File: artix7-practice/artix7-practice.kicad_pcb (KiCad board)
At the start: 2 copper layers, 49 parts, among them J101 USB_B_Micro, J102 Conn_02x06_Odd_Even, Q101 Q_NMOS_GSD, U102 TLV62568DDC, U103 TLV62568DDC, U104 FT2232HL, U105 93CxxC, U106 W25Q128JVS, X101 125MHz, Y101 ABM8-272-T3

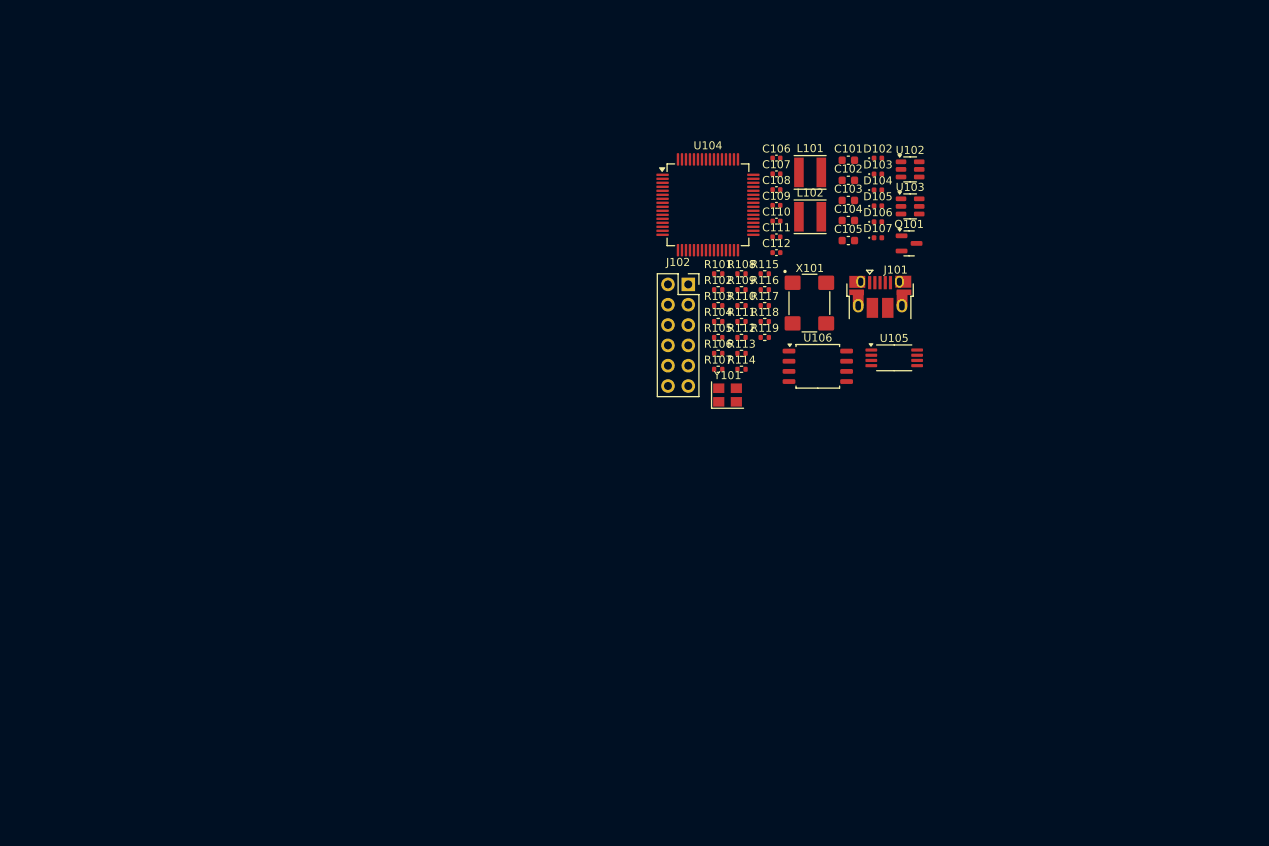
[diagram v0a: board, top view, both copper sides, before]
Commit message: Final version before switching from XC7A35T-xFTG256 to -xCSG325
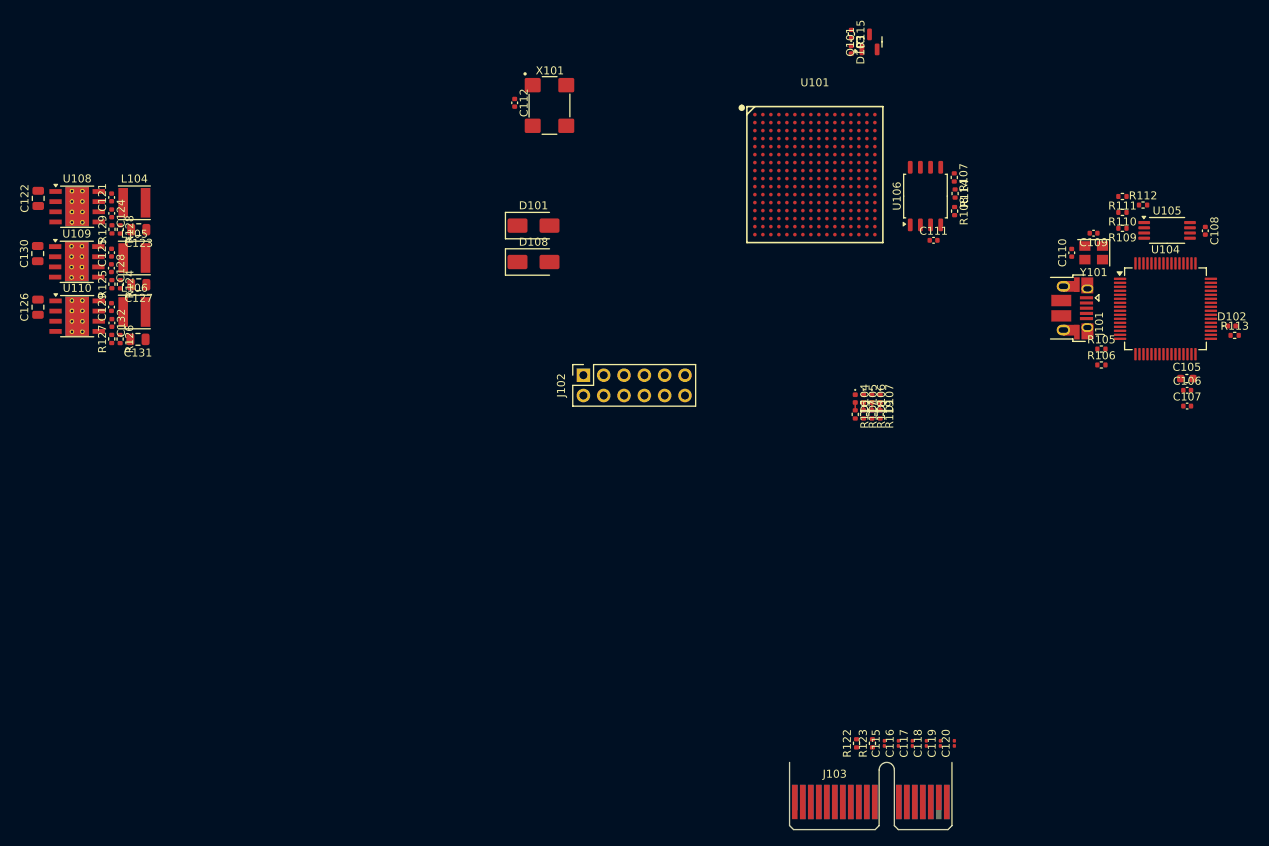
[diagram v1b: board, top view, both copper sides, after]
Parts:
- removed C101, C102, C103, C104: 22u, Capacitor_SMD:C_0603_1608Metric
- removed L101, L102: 2.2uH, Inductor_SMD:L_Taiyo-Yuden_NR-40xx
- removed R101: 39k, Resistor_SMD:R_0402_1005Metric
- removed R102: 62k, Resistor_SMD:R_0402_1005Metric
- removed R103: 68k, Resistor_SMD:R_0402_1005Metric
- removed R104: 33k, Resistor_SMD:R_0402_1005Metric
- removed U102, U103: TLV62568DDC, Package_TO_SOT_SMD:SOT-23-6
- added C115: 100n, Capacitor_SMD:C_0201_0603Metric, F.Cu at (63.3, 111.1)
- added C116: 100n, Capacitor_SMD:C_0201_0603Metric, F.Cu at (65.1, 111.1)
- added C117: 100n, Capacitor_SMD:C_0201_0603Metric, F.Cu at (66.8, 111.1)
- added C118: 100n, Capacitor_SMD:C_0201_0603Metric, F.Cu at (68.6, 111.1)
- added C119: 100n, Capacitor_SMD:C_0201_0603Metric, F.Cu at (70.3, 111.1)
- added C120: 100n, Capacitor_SMD:C_0201_0603Metric, F.Cu at (72.1, 111.1)
- added C121: 100n, Capacitor_SMD:C_0402_1005Metric, F.Cu at (-33.3, 42.9)
- added C122: 22u, Capacitor_SMD:C_0805_2012Metric, F.Cu at (-42.4, 43.0)
- added C123: 22u, Capacitor_SMD:C_0805_2012Metric, F.Cu at (-29.9, 46.9)
- added C124: 1u, Capacitor_SMD:C_0402_1005Metric, F.Cu at (-33.3, 44.9)
- added C125: 100n, Capacitor_SMD:C_0402_1005Metric, F.Cu at (-33.3, 49.8)
- added C126: 22u, Capacitor_SMD:C_0805_2012Metric, F.Cu at (-42.5, 56.6)
- added C127: 22u, Capacitor_SMD:C_0805_2012Metric, F.Cu at (-29.9, 53.8)
- added C128: 1u, Capacitor_SMD:C_0402_1005Metric, F.Cu at (-33.3, 51.7)
- added C129: 100n, Capacitor_SMD:C_0402_1005Metric, F.Cu at (-33.3, 56.6)
- added C130: 22u, Capacitor_SMD:C_0805_2012Metric, F.Cu at (-42.5, 49.9)
- added C131: 22u, Capacitor_SMD:C_0805_2012Metric, F.Cu at (-30.0, 60.6)
- added C132: 1u, Capacitor_SMD:C_0402_1005Metric, F.Cu at (-33.2, 58.6)
- added D101: MBRA340, Diode_SMD:D_SMA, F.Cu at (19.5, 46.4)
- added D108: MBRA340, Diode_SMD:D_SMA, F.Cu at (19.5, 51.0)
- added J103: Bus_PCI_Express_x1, Connector_PCBEdge:BUS_PCIexpress_x1, F.Cu at (52.1, 118.5)
- added L104: 2.2uH, Inductor_SMD:L_Taiyo-Yuden_NR-40xx, F.Cu at (-30.4, 43.6)
- added L105: 2.2uH, Inductor_SMD:L_Taiyo-Yuden_NR-40xx, F.Cu at (-30.4, 50.5)
- added L106: 2.2uH, Inductor_SMD:L_Taiyo-Yuden_NR-40xx, F.Cu at (-30.4, 57.2)
- added R122: 4.7k, Resistor_SMD:R_0402_1005Metric, F.Cu at (59.8, 111.1)
- added R123: 4.7k, Resistor_SMD:R_0402_1005Metric, F.Cu at (61.8, 111.1)
- added R124: 43k, Resistor_SMD:R_0402_1005Metric, F.Cu at (-32.2, 53.8)
- added R125: 56k, Resistor_SMD:R_0402_1005Metric, F.Cu at (-33.2, 53.7)
- added R126: 68k, Resistor_SMD:R_0402_1005Metric, F.Cu at (-32.2, 60.6)
- added R127: 30k, Resistor_SMD:R_0402_1005Metric, F.Cu at (-33.3, 60.6)
- added R128: 1k, Resistor_SMD:R_0402_1005Metric, F.Cu at (-32.2, 46.9)
- added R129: 150k, Resistor_SMD:R_0402_1005Metric, F.Cu at (-33.2, 46.9)
- added U101: XC7A35T-FTG256, easyeda2kicad:FBGA-256_L17.0-W17.0-R16-C16-P1.00-TL, F.Cu at (54.6, 40.0)
- added U108: LMR33630ADDA, Package_SO:Texas_HSOP-8-1EP_3.9x4.9mm_P1.27mm_ThermalVias, F.Cu at (-37.6, 44.1)
- added U109: LMR33630ADDA, Package_SO:Texas_HSOP-8-1EP_3.9x4.9mm_P1.27mm_ThermalVias, F.Cu at (-37.6, 51.0)
- added U110: LMR33630ADDA, Package_SO:Texas_HSOP-8-1EP_3.9x4.9mm_P1.27mm_ThermalVias, F.Cu at (-37.6, 57.7)
- moved R113 61.7 mm to (107.1, 60.1)
- moved C106 59.0 mm to (101.2, 67.0)
- moved C107 59.0 mm to (101.2, 69.0)
- moved U104 58.6 mm to (98.5, 56.8)
- moved C108 53.9 mm to (103.4, 47.1), turned to -90 degrees
- moved R112 52.9 mm to (95.7, 43.9)
- moved R111 50.1 mm to (93.1, 42.8), turned to 180 degrees
- moved Y101 49.1 mm to (89.5, 49.8), turned to 180 degrees
- moved R110 49.0 mm to (93.1, 44.8), turned to 180 degrees
- moved D102 49.0 mm to (106.8, 59.0)
- moved R109 48.2 mm to (93.1, 46.8), turned to 180 degrees
- moved R105 47.9 mm to (90.5, 61.9)
- moved R106 47.9 mm to (90.5, 63.8)
- moved C105 45.7 mm to (101.1, 65.5)
- moved X101 40.8 mm to (21.5, 31.4)
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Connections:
- J101 pad 1: +5V -> VBUS
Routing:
- net Net-(D107-A): track 0.00 -> 0.98 mm
- net Net-(D106-A): track 0.00 -> 0.98 mm
- net Net-(D105-A): track 0.00 -> 0.98 mm
- net Net-(D104-A): track 0.00 -> 0.98 mm
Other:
- board outline added: 20.3 x 8.4 mm

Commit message: JLCPCB uploads
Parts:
- added C101: 100n, Capacitor_SMD:C_0402_1005Metric, F.Cu at (71.0, 77.8)
- added C102: 22u, Capacitor_SMD:C_0805_2012Metric, F.Cu at (61.8, 77.9)
- added C103: 22u, Capacitor_SMD:C_0805_2012Metric, F.Cu at (74.3, 81.8)
- added C104: 1u, Capacitor_SMD:C_0402_1005Metric, F.Cu at (71.0, 79.8)
- added C113: 22u, Capacitor_SMD:C_0603_1608Metric, B.Cu at (82.4, 89.9)
- added C114: 22u, Capacitor_SMD:C_0603_1608Metric, B.Cu at (82.4, 93.6)
- added C133: 1u, Capacitor_SMD:C_0201_0603Metric, B.Cu at (87.9, 91.3)
- added C134: 1u, Capacitor_SMD:C_0201_0603Metric, B.Cu at (88.7, 93.7)
- added C135: 1u, Capacitor_SMD:C_0201_0603Metric, B.Cu at (85.5, 94.5)
- added C136: 1u, Capacitor_SMD:C_0201_0603Metric, B.Cu at (84.7, 92.1)
- added C137: 1u, Capacitor_SMD:C_0201_0603Metric, B.Cu at (85.5, 91.3)
- added C138: 100n, Capacitor_SMD:C_0201_0603Metric, B.Cu at (87.1, 91.3)
- added C139: 1u, Capacitor_SMD:C_0201_0603Metric, B.Cu at (93.9, 86.9)
- added C140: 100n, Capacitor_SMD:C_0201_0603Metric, B.Cu at (87.1, 94.5)
- added C141: 100n, Capacitor_SMD:C_0201_0603Metric, B.Cu at (83.9, 93.7)
- added C142: 1u, Capacitor_SMD:C_0201_0603Metric, B.Cu at (87.9, 92.9)
- added C143: 1u, Capacitor_SMD:C_0201_0603Metric, B.Cu at (90.7, 86.9)
- added C144: 100n, Capacitor_SMD:C_0201_0603Metric, B.Cu at (93.1, 87.7)
- added C145: 100n, Capacitor_SMD:C_0201_0603Metric, B.Cu at (88.3, 87.7)
- added C146: 1u, Capacitor_SMD:C_0201_0603Metric, B.Cu at (87.5, 86.9)
- added C147: 1u, Capacitor_SMD:C_0201_0603Metric, B.Cu at (89.1, 89.3)
- added C148: 100n, Capacitor_SMD:C_0201_0603Metric, B.Cu at (93.1, 90.1)
- added C149: 100n, Capacitor_SMD:C_0201_0603Metric, B.Cu at (88.3, 90.1)
- added C150: 1u, Capacitor_SMD:C_0201_0603Metric, B.Cu at (93.1, 89.3)
- added C151: 1u, Capacitor_SMD:C_0201_0603Metric, B.Cu at (91.5, 89.3)
- added C152: 100n, Capacitor_SMD:C_0201_0603Metric, B.Cu at (90.7, 90.1)
- added C153: 100n, Capacitor_SMD:C_0201_0603Metric, B.Cu at (92.3, 86.1)
- added C154: 1u, Capacitor_SMD:C_0201_0603Metric, B.Cu at (89.1, 85.3)
- added C155: 1u, Capacitor_SMD:C_0201_0603Metric, B.Cu at (90.7, 85.3)
- added C156: 1u, Capacitor_SMD:C_0201_0603Metric, B.Cu at (93.9, 85.3)
- added C157: 100n, Capacitor_SMD:C_0201_0603Metric, B.Cu at (92.3, 85.3)
- added C158: 1u, Capacitor_SMD:C_0201_0603Metric, B.Cu at (89.9, 87.7)
- added C159: 1u, Capacitor_SMD:C_0201_0603Metric, B.Cu at (95.5, 86.9)
- added C160: 1u, Capacitor_SMD:C_0201_0603Metric, B.Cu at (86.7, 86.1)
- added C161: 1u, Capacitor_SMD:C_0201_0603Metric, B.Cu at (94.3, 89.7)
- added C162: 22u, Capacitor_SMD:C_0603_1608Metric, B.Cu at (96.8, 91.3)
- added C163: 22u, Capacitor_SMD:C_0603_1608Metric, B.Cu at (92.1, 92.9)
- added C164: 22u, Capacitor_SMD:C_0603_1608Metric, B.Cu at (85.9, 82.8)
- added C165: 22u, Capacitor_SMD:C_0603_1608Metric, B.Cu at (93.9, 82.8)
- added L101: 2.2uH, Inductor_SMD:L_Taiyo-Yuden_NR-40xx, F.Cu at (73.8, 78.5)
- added L102: 2.2uH, Inductor_SMD:L_Taiyo-Yuden_NR-40xx, F.Cu at (79.5, 89.1)
- added L103: 2.2uH, Inductor_SMD:L_Taiyo-Yuden_NR-40xx, F.Cu at (79.4, 94.3)
- added R101: 18k, Resistor_SMD:R_0402_1005Metric, F.Cu at (72.1, 81.8)
- added R102: 82k, Resistor_SMD:R_0402_1005Metric, F.Cu at (71.0, 81.8)
- added R103: 100, Resistor_SMD:R_0402_1005Metric, B.Cu at (80.7, 89.9)
- added U102: XC7A35T-CSG325, Package_BGA:Xilinx_CSG325, F.Cu at (90.7, 88.1)
- C105, C106, C107, C109, C110, C111, C115, C116, C119, C120, R107, R108, R109, R111, R112, R114, X101, Y101: moved to B.Cu
- U101: value XC7A35T-FTG256 -> LMR33630ADDA; footprint easyeda2kicad:FBGA-256_L17.0-W17.0-R16-C16-P1.00-TL -> Package_SO:Texas_HSOP-8-1EP_3.9x4.9mm_P1.27mm_ThermalVias
- moved C126 109.8 mm to (61.7, 91.3)
- moved C127 109.8 mm to (74.3, 88.5)
- moved C128 109.8 mm to (70.9, 86.4)
- moved C129 109.8 mm to (70.9, 91.3)
- moved C130 109.8 mm to (61.7, 84.6)
- moved C132 109.8 mm to (71.0, 93.3)
- moved L105 109.8 mm to (73.8, 85.2)
- moved L106 109.8 mm to (73.8, 91.9)
- moved R124 109.8 mm to (72.0, 88.5)
- moved R125 109.8 mm to (71.0, 88.4)
- moved R126 109.8 mm to (72.0, 95.3)
- moved U109 109.8 mm to (66.6, 85.7)
- moved U110 109.8 mm to (66.6, 92.4)
- moved C125 109.8 mm to (70.9, 84.5)
- moved C131 109.8 mm to (74.2, 95.3)
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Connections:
- net Net-(J103-PERn0) renamed /PCIE_TX0_PRE-
- net Net-(J103-PERp0) renamed /PCIE_TX0_PRE+
- net Net-(J103-PETn0) renamed /PCIE_RX0_PRE-
- net Net-(J103-PETp0) renamed /PCIE_RX0_PRE+
- net Net-(J103-REFCLK+) renamed /REFCLK_PRE+
- net Net-(J103-REFCLK-) renamed /REFCLK_PRE-
- D101 pad 1: /POWER -> /MAIN_PWR
- D108 pad 1: /POWER -> /MAIN_PWR
- U108 pad 4: Net-(U108-PG) -> Net-(U101-EN)
- U109 pad 3: Net-(U108-PG) -> Net-(U101-EN)
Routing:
- net GND: track 0.00 -> 99.0 mm, vias 0 -> 127
- net /MAIN_PWR: track 0.00 -> 93.6 mm
- net +1V8: track 0.00 -> 63.2 mm, vias 0 -> 9
- net +3V3: track 0.00 -> 52.5 mm, vias 0 -> 42
- net +1V0: track 0.00 -> 49.2 mm, vias 0 -> 24
- net /JTAG_TMS: track 0.00 -> 47.7 mm, vias 0 -> 4
- net /JTAG_TDI: track 0.00 -> 47.2 mm, vias 0 -> 4
- net /JTAG_TDO: track 0.00 -> 46.3 mm, vias 0 -> 4
- net /GPIO0: track 0.00 -> 43.6 mm, vias 0 -> 1
- net /GPIO4: track 0.00 -> 43.5 mm, vias 0 -> 1
- net /GPIO5: track 0.00 -> 41.2 mm, vias 0 -> 1
- net /GPIO1: track 0.00 -> 40.0 mm, vias 0 -> 1
- net /GPIO6: track 0.00 -> 39.1 mm, vias 0 -> 1
- net /LED1: track 0.00 -> 38.1 mm, vias 0 -> 2
- net /LED2: track 0.00 -> 37.1 mm, vias 0 -> 2
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- added copper zone on F.Cu, net +12V
- added copper zone on In2.Cu, net +1V0
- added copper zone on In4.Cu, net +3V3
- added copper zone on In1.Cu, net GND
- added copper zone on In3.Cu, net GND
- added copper zone on In6.Cu, net GND
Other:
- board size 20.3 x 8.4 mm -> 41 x 48.1 mm
- copper layers 2 -> 8
- board text added: "3V3"
- board text added: "4 0 5 1 6 2 7 3"
- board text added: "Artix-7 Test Board Peter Schmidt-Nielsen Saturn Data"
- board text added: "Artix-7 Test Board Saturn Data ©2024"
- board text added: "Done"
- board text added: "GND"
- board text added: "LED0"
- board text added: "LED1"
- board text added: "LED2"
- board text added: "LED3"
- board text added: "USB Err"
